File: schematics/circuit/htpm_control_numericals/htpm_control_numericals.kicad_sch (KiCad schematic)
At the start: 26 parts, among them J1 Conn_01x05_Socket, U1 MAX7219, U10 D168K, U11 D168K, U12 D168K, U13 MAX7219, U14 D168K, U15 D168K, U16 D168K, U17 D168K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

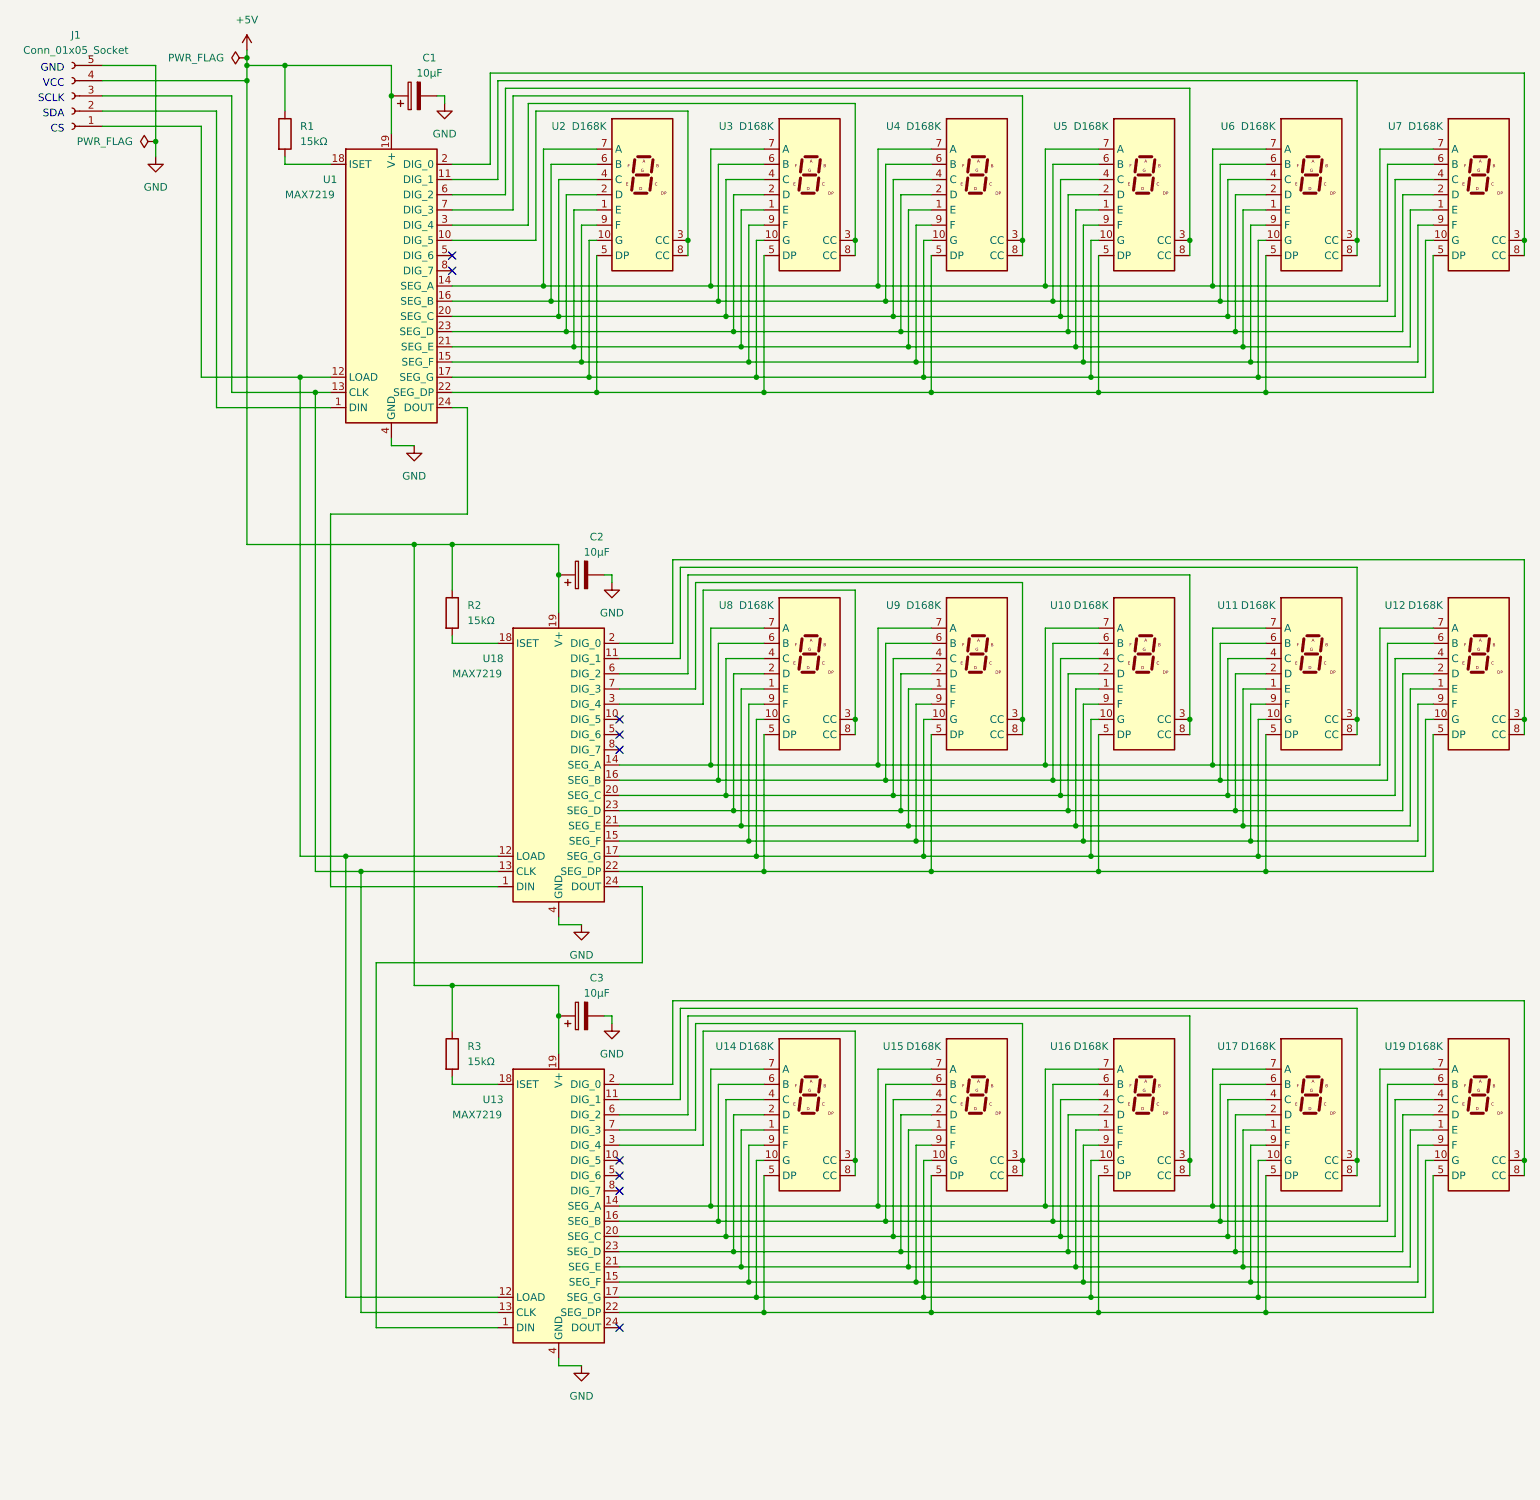
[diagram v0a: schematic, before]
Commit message: Added footprints to the PCB design.
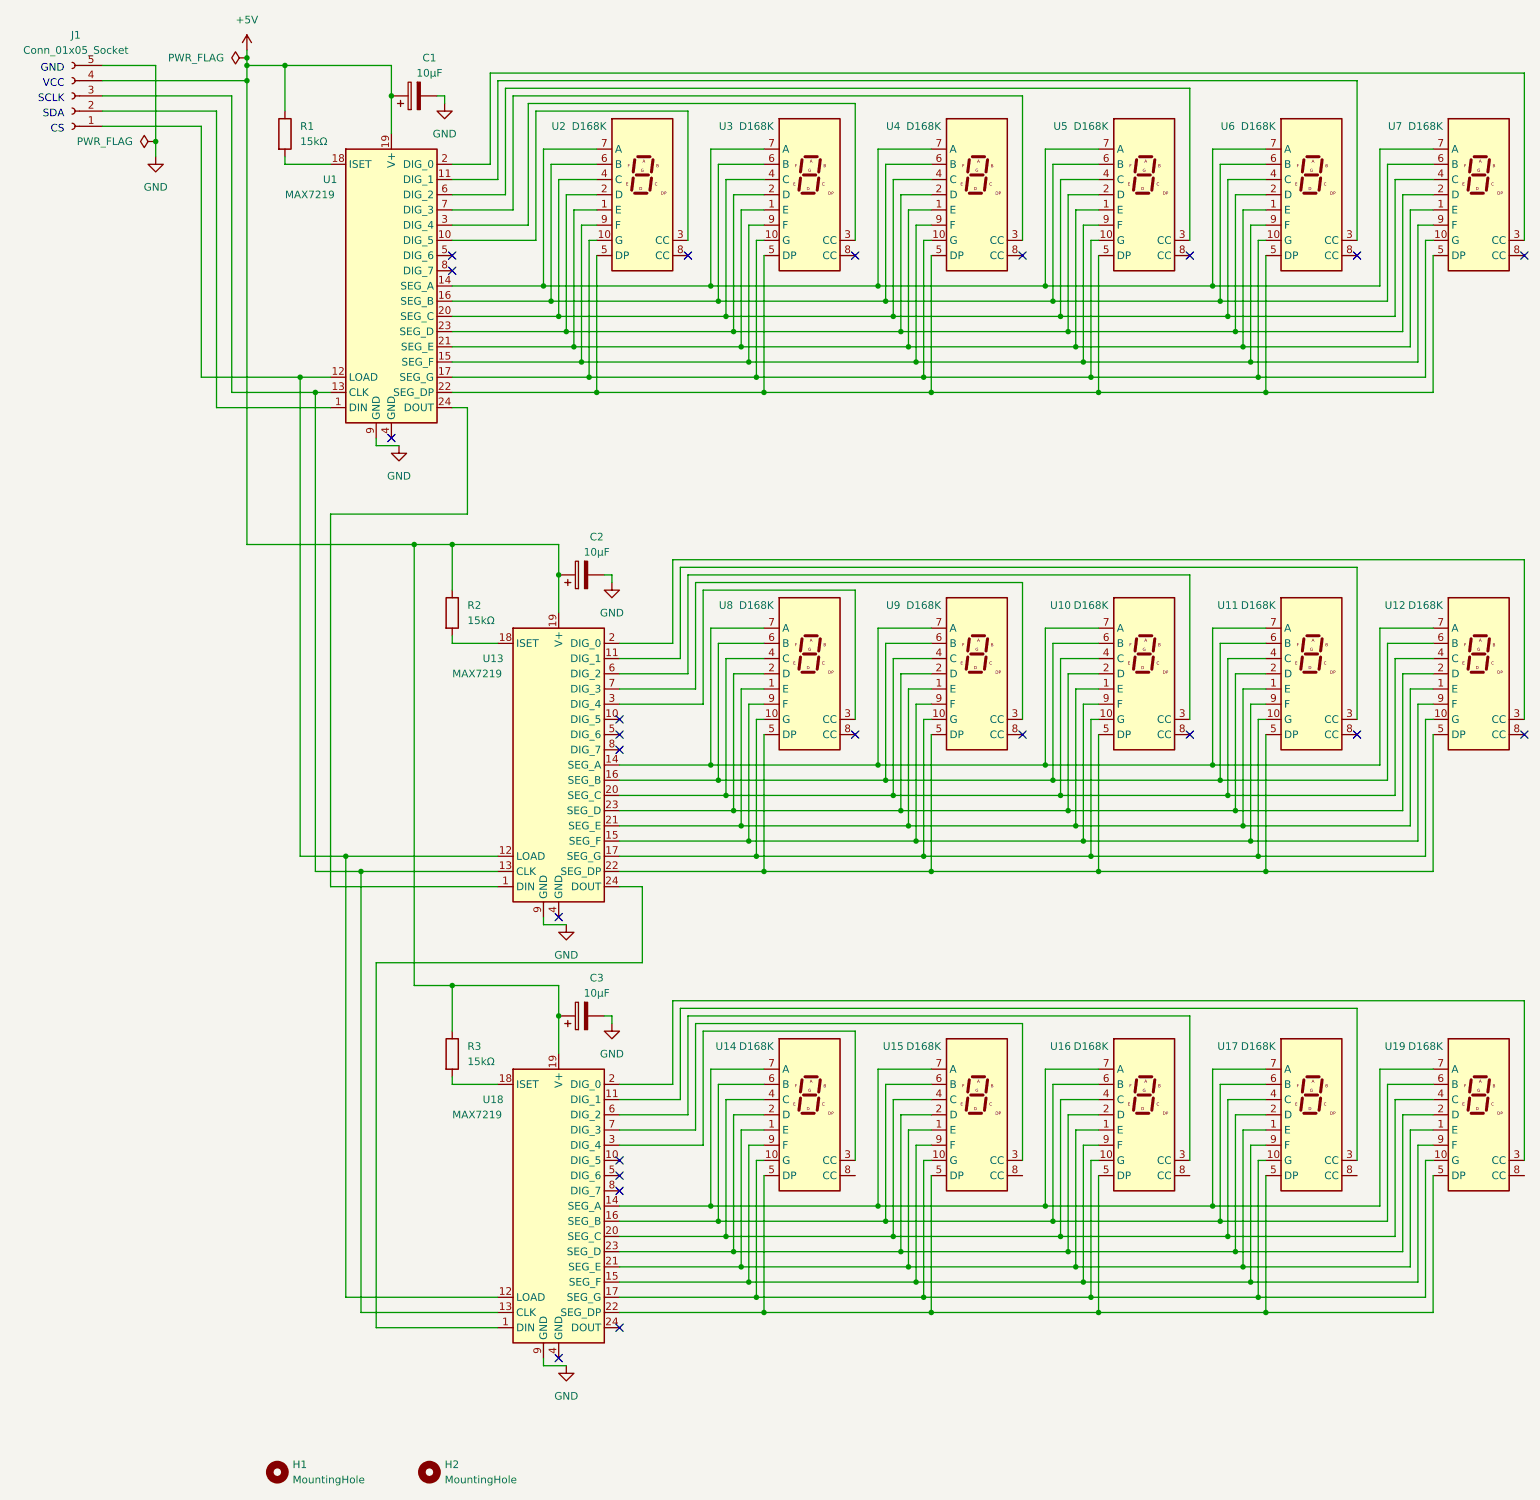
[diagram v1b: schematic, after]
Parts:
- added H1, H2: MountingHole, MountingHole:MountingHole_2.5mm, symbol Mechanical:MountingHole
- renumbered U18 to U13, U13 to U18
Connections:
- net GND: no longer U1.4 (GND), U13.4 (GND), U18.4 (GND)
- net at U11.3 (CC), U13.11 (DIG_1): no longer U11.8 (CC)
- net at U1.6 (DIG_2), U5.3 (CC): no longer U5.8 (CC)
- net at U1.2 (DIG_0), U7.3 (CC): no longer U7.8 (CC)
- net at U13.7 (DIG_3), U9.3 (CC): no longer U9.8 (CC)
- net at U10.3 (CC), U13.6 (DIG_2): no longer U10.8 (CC)
- net at U1.11 (DIG_1), U6.3 (CC): no longer U6.8 (CC)
- net at U17.3 (CC), U18.11 (DIG_1): no longer U17.8 (CC)
- net at U18.2 (DIG_0), U19.3 (CC): no longer U19.8 (CC)
- net at U14.3 (CC), U18.3 (DIG_4): no longer U14.8 (CC)
- net at U16.3 (CC), U18.6 (DIG_2): no longer U16.8 (CC)
- net at U15.3 (CC), U18.7 (DIG_3): no longer U15.8 (CC)
- net at U12.3 (CC), U13.2 (DIG_0): no longer U12.8 (CC)
- net at U13.3 (DIG_4), U8.3 (CC): no longer U8.8 (CC)
- net at U1.10 (DIG_5), U2.3 (CC): no longer U2.8 (CC)
- net at U1.3 (DIG_4), U3.3 (CC): no longer U3.8 (CC)
- net at U1.7 (DIG_3), U4.3 (CC): no longer U4.8 (CC)
- no-connect marks 9 -> 23

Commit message: Updated nominal values.
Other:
- note added: "5V"
- note removed: "VCC"
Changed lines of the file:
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@@
     (stroke (width 0) (type default))
   )
-  (text "VCC" (at 58.42 38.1 0)
+  (text "5V" (at 58.42 38.1 0)
     (effects (font (size 1.27 1.27)) (justify right bottom))
   )
